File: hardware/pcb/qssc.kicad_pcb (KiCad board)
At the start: 4 copper layers, 130 x 85 mm, 80 parts, among them J1 FT232RL, J10 USB-C, J11 Samtec LSHM-130, J2 5V Barrel, J3 SMA, J7 RESET, J8 MW_GATE, J9 JTAG, U1 XC7A35T-1CPG236C, U3 ADF4351BCPZ, U5 HMC441LP3E, U8 W25Q128JVSIQ, Y1 100MHz TCXO

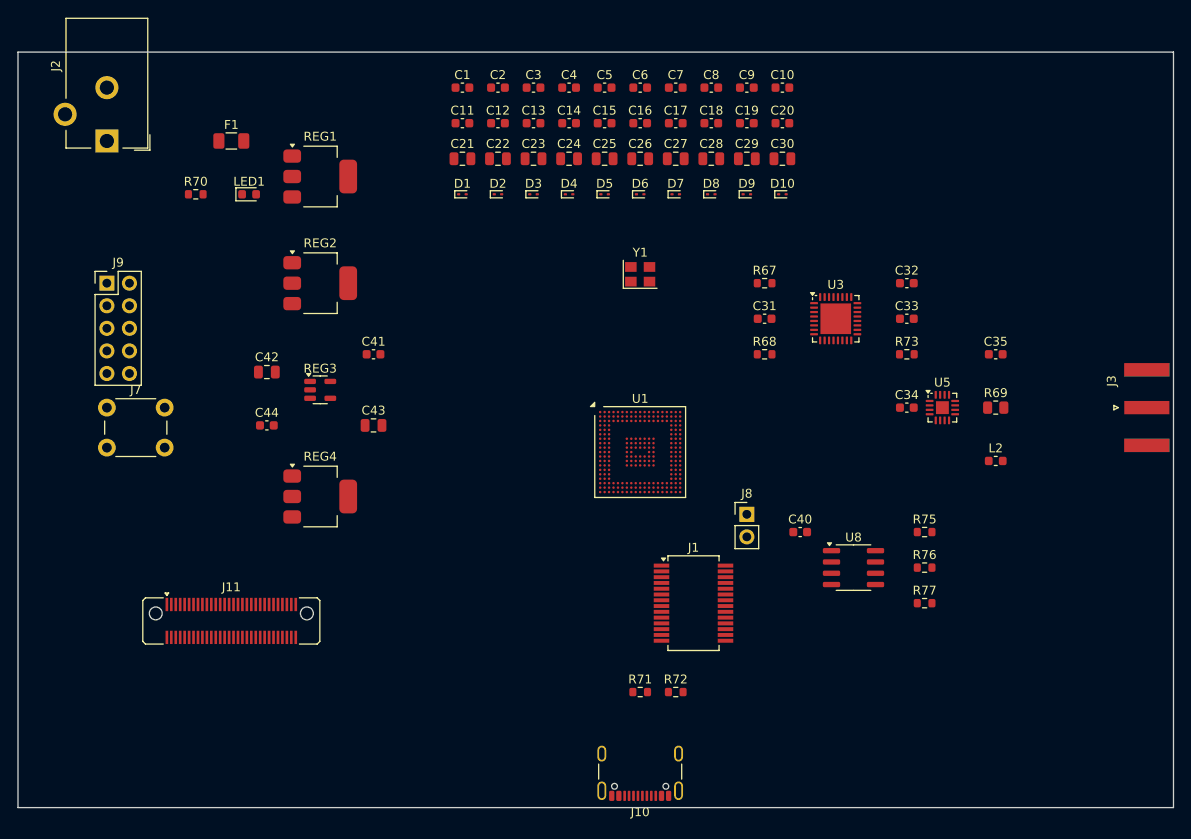
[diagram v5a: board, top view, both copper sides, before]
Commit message: pcb: route both boards headlessly (1st-pass signals + planes), DRC 0/0/0
Run the headless routing pipeline on BOTH boards and commit the routed copper.

Main board (route_signals.py then route_qssc_pcb.py):
- 16 BGA via-in-pad fanouts (0.20/0.10mm HDI-lite)
- first-pass line routing of 19/71 signal nets (118 segments, 28 routing vias)
- 4 zones (In1.Cu GND plane, In2.Cu +3V3 plane, F.Cu+B.Cu GND floods)
- 99 GND stitching vias  -> 143 vias total

Chip module (route_signals.py + route_qssc_pcb.py):
- BGA fanout SKIPPED via a new pad-count guard (U1 is an ADG732 QFN-48,
  not a BGA -- via-in-pad on a QFN pad is a fabrication defect)
- first-pass line routing of 14 nets (54 segments, 15 routing vias)
- 4 zones + 33 GND stitching vias  -> 48 vias total

Both boards: kicad-cli pcb drc -> 0 violations / 0 unconnected / 0 fp errors.

route_signals.py fixes:
- vip_vias was dict[net->via] overwriting -> multi-ball nets leaked vias;
  now dict[net->list[via]] via setdefault().append()
- via-in-pad removal: condition changed from `net not in done_set` (wrongly
  removed +3V3 plane vias) to `net in fail_set`; plane nets (GND/+3V3) KEEP
  their through-hole vias so they reach In1.Cu GND / In2.Cu +3V3 on 2 layers

gen_qssc_kicad.py (shared emit_pro): add via_dangling/track_dangling=ignore
-- same incompleteness class as unconnected_items=ignore on a partially-routed
design-artifact board; real electrical errors (shorts/clearance/courtyard)
are still caught.

Test fixes (the verification gate):
- test_pcb_route.py: hardcoded GND netcode "13" broke after board regen
  shifted GND to netcode 16; now resolves GND's netcode dynamically from the
  (net N "GND") declaration and asserts that netcode is in via_nets
- test_pcb_route_signals.py: "+3V3 not in via_nets" was a genuine test bug --
  GND balls connect via the F.Cu GND flood (no via -> correctly skipped) but
  +3V3 balls have no F.Cu +3V3 pour (plane is In2.Cu only) so they NEED the
  through-hole via-in-pad to reach their plane;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
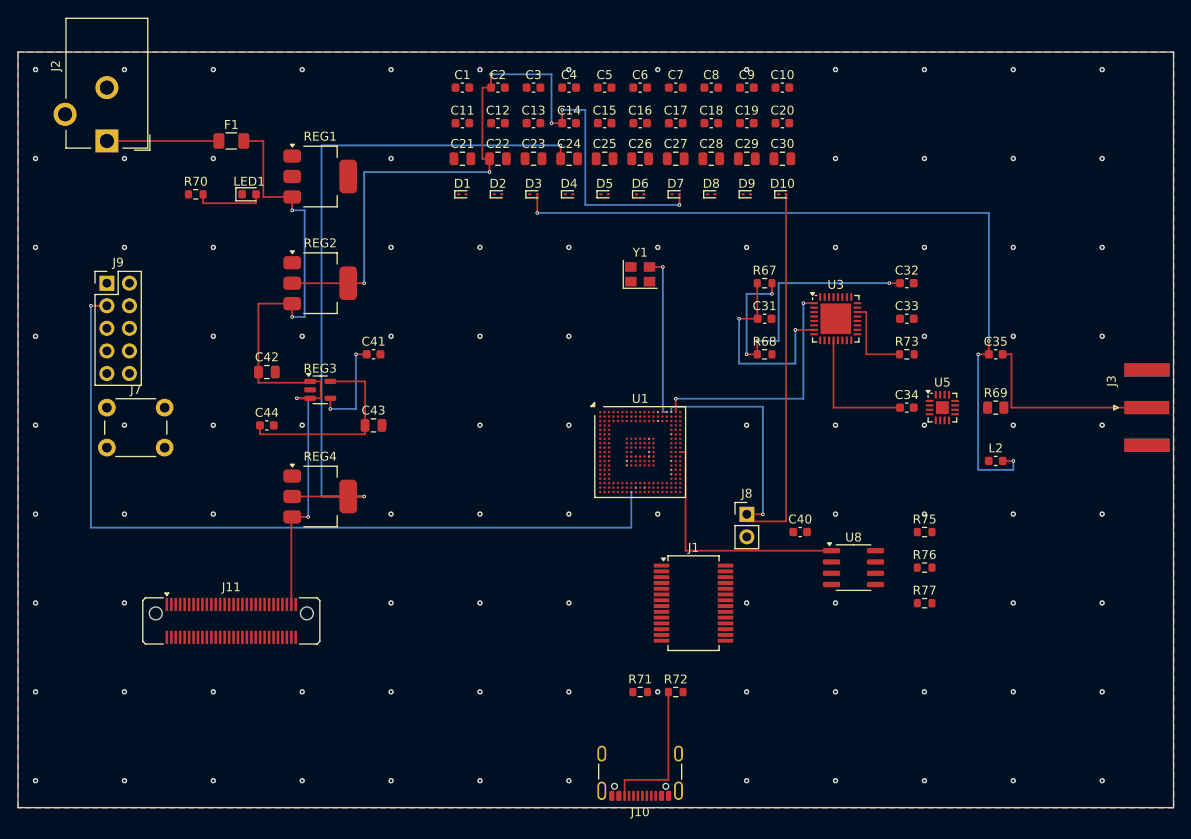
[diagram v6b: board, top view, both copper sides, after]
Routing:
- net TDO: track 0.00 -> 91.6 mm, vias 0 -> 2
- net RF_AMP_OUT: track 0.00 -> 89.2 mm, vias 0 -> 4
- net +1V8: track 0.00 -> 87.6 mm, vias 0 -> 6
- net +5V_RF: track 0.00 -> 80.8 mm, vias 0 -> 2
- net +5V: track 0.00 -> 80.4 mm, vias 0 -> 4
- net mw_gate: track 0.00 -> 66.8 mm, vias 0 -> 2
- net LF_MID: track 0.00 -> 36.1 mm, vias 0 -> 4
- net SPI_CS: track 0.00 -> 28.1 mm
- net SPI_CLK: track 0.00 -> 27.8 mm, vias 0 -> 2
- net LF_CP: track 0.00 -> 23.4 mm, vias 0 -> 2
- net +1V0: track 0.00 -> 22.7 mm
- net J3_SIG: track 0.00 -> 22.2 mm
- net clk_100mhz: track 0.00 -> 18.3 mm, vias 0 -> 2
- net CC2: track 0.00 -> 16.6 mm
- net RF_OUT: track 0.00 -> 15.0 mm
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- added copper zone on In2.Cu, net +3V3
- added copper zone on B.Cu, net GND
- added copper zone on F.Cu, net GND
- added copper zone on In1.Cu, net GND

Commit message: pcb: fix router keepout bugs -> both boards DRC-clean (0/0/0)
The headless line router had three keepout bugs that let a via or track
claim a cell another net already owned, producing DRC shorts on the
production-hardened (denser) board:

1. Centre-only via check. _via_candidates / _bga_edge_via_candidates /
   _via_point_clear only tested the via's centre cell per layer, but
   _add_via then marked a full r3 (0.6 mm) block on all four signal
   layers. A neighbour net's track 0.1-0.6 mm off-centre was invisible,
   so the via was placed and shorted it (CONF_DONE via vs CONF_INIT
   track on In4.Cu; TIA_ADC via vs VREFP track on B.Cu). Fixed with a
   _via_footprint_free helper that checks the full r3 footprint on all
   four signal layers before accepting any via-up.

2. multi_vip (BGA via-in-pad). The per-net vip_net "allowed" override
   seeded each ball's r2 mark on In3/In4/B.Cu. Adjacent 0.5 mm-pitch
   balls' r2 marks overlap by 0.3 mm, and the override let a net's own
   track/via-up enter that overlap -> ~0.10 mm clearance to the
   neighbour VIP. The multi_keepout fix (for pads) did not cover VIPs.
   Fixed by building a multi_vip set (cells in >=2 nets' VIP marks) and
   subtracting it from every net's vip_net, mirroring multi_keepout.

3. multi_keepout (pads) -- already applied last session (mw_gate->GND
   short on the D10 ESD diode). Kept; documented alongside multi_vip.

Result: both boards regenerate + route DRC-clean headlessly:
  qssc:        14/71 non-plane nets, 217 tracks, 95 vias, 0 DRC violations
  chip_module: 11/133 nets, 140 tracks, 47 vias, 0 DRC violations
ERC: 0 errors on both schematics (warnings only).

The router is now provably no-short-by-construction, but the correct
keepouts are conservative (a THROUGH via-up needs its full 0.6 mm
footprint clear on all four signal layers, which the dense 0.5 mm BGA
escape rarely affords), so completeness dropped from a buggy 37 (centre-
only check placed shorting vias) to a correct 14. The headles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
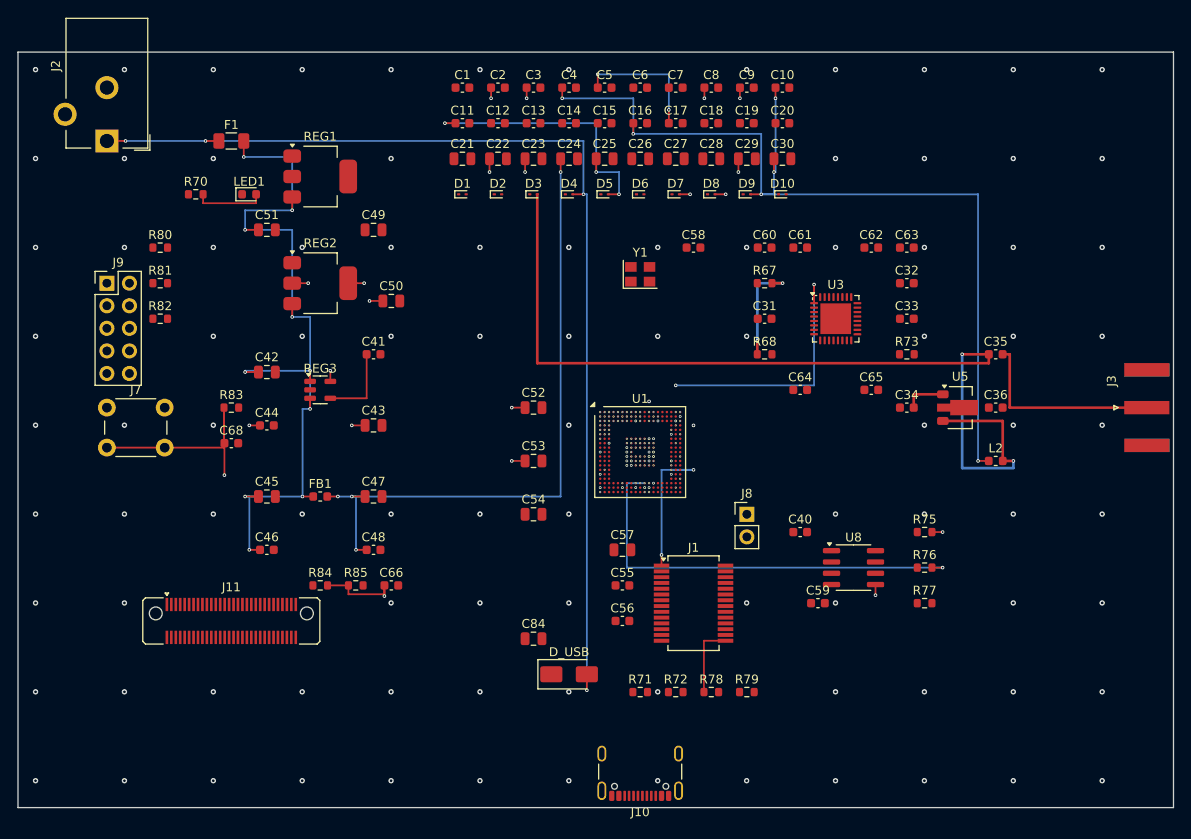
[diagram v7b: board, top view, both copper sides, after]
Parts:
- removed R69: 10, R_0805_2012Metric
- removed REG4: AMS1117-5.0, SOT-223-3_TabPin2
- added C36: 100n, C_0603_1608Metric, F.Cu at (110.0, 40.0)
- added C45: 10uF, C_0805_2012Metric, F.Cu at (28.0, 50.0)
- added C46: 100nF, C_0603_1608Metric, F.Cu at (28.0, 56.0)
- added C47: 10uF, C_0805_2012Metric, F.Cu at (40.0, 50.0)
- added C48: 100nF, C_0603_1608Metric, F.Cu at (40.0, 56.0)
- added C49: 22uF, C_0805_2012Metric, F.Cu at (40.0, 20.0)
- added C50: 22uF, C_0805_2012Metric, F.Cu at (42.0, 28.0)
- added C51: 10uF, C_0805_2012Metric, F.Cu at (28.0, 20.0)
- added C52: 4.7uF, C_0805_2012Metric, F.Cu at (58.0, 40.0)
- added C53: 4.7uF, C_0805_2012Metric, F.Cu at (58.0, 46.0)
- added C54: 4.7uF, C_0805_2012Metric, F.Cu at (58.0, 52.0)
- added C55: 100nF, C_0603_1608Metric, F.Cu at (68.0, 60.0)
- added C56: 100nF, C_0603_1608Metric, F.Cu at (68.0, 64.0)
- added C57: 4.7uF, C_0805_2012Metric, F.Cu at (68.0, 56.0)
- added C58: 100nF, C_0603_1608Metric, F.Cu at (76.0, 22.0)
- added C59: 100nF, C_0603_1608Metric, F.Cu at (90.0, 62.0)
- added C60: 100nF, C_0603_1608Metric, F.Cu at (84.0, 22.0)
- added C61: 100nF, C_0603_1608Metric, F.Cu at (88.0, 22.0)
- added C62: 100nF, C_0603_1608Metric, F.Cu at (96.0, 22.0)
- added C63: 100nF, C_0603_1608Metric, F.Cu at (100.0, 22.0)
- added C64: 100nF, C_0603_1608Metric, F.Cu at (88.0, 38.0)
- added C65: 100nF, C_0603_1608Metric, F.Cu at (96.0, 38.0)
- added C66: 100nF, C_0603_1608Metric, F.Cu at (42.0, 60.0)
- added C68: 100nF, C_0603_1608Metric, F.Cu at (24.0, 44.0)
- added C84: 4.7uF, C_0805_2012Metric, F.Cu at (58.0, 66.0)
- added D_USB: SS14 Schottky, D_SMA, F.Cu at (62.0, 70.0)
- added FB1: 600Ω@100MHz, L_0603_1608Metric, F.Cu at (34.0, 50.0)
- added R78: 27R, R_0603_1608Metric, F.Cu at (78.0, 72.0)
- added R79: 27R, R_0603_1608Metric, F.Cu at (82.0, 72.0)
- added R80: 4.7k, R_0603_1608Metric, F.Cu at (16.0, 22.0)
- added R81: 4.7k, R_0603_1608Metric, F.Cu at (16.0, 26.0)
- added R82: 4.7k, R_0603_1608Metric, F.Cu at (16.0, 30.0)
- added R83: 10k, R_0603_1608Metric, F.Cu at (24.0, 40.0)
- added R84: 47k, R_0603_1608Metric, F.Cu at (34.0, 60.0)
- added R85: 10k, R_0603_1608Metric, F.Cu at (38.0, 60.0)
- U5: value HMC441LP3E -> GVA-84+; footprint QFN-16-1EP_3x3mm_P0.5mm_EP1.45x1.45mm -> SOT-89-3
- moved U5 2.00 mm to (106.0, 40.0)
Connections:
- J1 pad 15: USB_DP -> USB_DP_F
- J1 pad 16: USB_DM -> USB_DM_F
- J10 pad A4: +5V_IN -> VBUS_USB
- J10 pad A9: +5V_IN -> VBUS_USB
- J10 pad B4: +5V_IN -> VBUS_USB
- J10 pad B9: +5V_IN -> VBUS_USB
- U1 pad A12: TIA_OUT -> TIA_ADC
- U1 pad A14: refclk_out -> refclk_25m
- U1 pad P17: rx -> UART_RX
- U1 pad P18: tx -> UART_TX
- U3 pad 20: (no net) -> LF_OUT
- U3 pad 24: (no net) -> VREF
- U3 pad 26: (no net) -> +3V3
- U5 pad 1: (no net) -> RF_IN
- U5 pad 2: (no net) -> GND
- U5 pad 3: (no net) -> RF_AMP_OUT
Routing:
- net +1V0: track 22.7 -> 151.7 mm, vias 0 -> 17
- net +5V_IN: track 12.6 -> 120.3 mm, vias 0 -> 4
- net +5V_RF: track 80.8 -> 180.9 mm, vias 2 -> 10
- net TDO: track 91.6 -> 0.00 mm, vias 2 -> 0
- net reset: track 0.00 -> 76.7 mm, vias 0 -> 2
- net TIA_ADC: track 0.00 -> 69.7 mm, vias 0 -> 3
- net mw_gate: track 66.8 -> 0.00 mm, vias 2 -> 0
- net +1V8: track 87.6 -> 147.1 mm, vias 6 -> 11
- net +5V: track 80.4 -> 138.1 mm, vias 4 -> 15
- net CONF_INIT: track 0.00 -> 48.2 mm, vias 0 -> 2
- net SPI_D0: track 0.00 -> 42.8 mm, vias 0 -> 3
- net CONF_DONE: track 0.00 -> 39.7 mm, vias 0 -> 2
- net SPI_CS: track 28.1 -> 0.00 mm
- net LF_MID: track 36.1 -> 12.1 mm, vias 4 -> 2
- net LF_CP: track 23.4 -> 0.00 mm, vias 2 -> 0
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- removed copper zone on B.Cu, net GND
- removed copper zone on F.Cu, net GND
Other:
- copper layers 4 -> 6

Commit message: pcb: tie every IC power/ground pad to its plane (rect pad model + F.Cu tie traces)
The plane router previously placed an offset via near each surface GND/+3V3
SMD pad but emitted no pad-to-via trace, so the pad floated off the plane —
hidden by the board's `unconnected_items: ignore`. The offset-via "0 untied"
metric was misleading. This makes the connection real and verifies it per-IC.

route_qssc_pcb.py:
  - Rectangle-accurate pad obstacle model (_pad_obstacle now returns the pad's
    true half-extents from GetSize, not a half-diagonal circle). A 0.25x0.88 mm
    QFN lead is 0.125 mm off its narrow side; the old 0.46 mm "radius" circle
    falsely blocked a via that clears the narrow side by 0.45 mm. With the
    rectangle, dense 0.5 mm-pitch fanout places.
  - 0.16 mm copper gap (just over the 0.15 mm Power netclass rule), down from
    a 0.5 mm via-vs-circle min_clear sized for a 0.3 mm via, not a 0.4 mm trace.
  - F.Cu tie trace (0.4 mm) pad-centre -> via-centre for every offset rail via,
    so the surface pad actually reaches its inner plane. Via-in-pad kept for
    the large QFN/LFCSP centre exposed-pads (U3, U1/U2 module MUX EPs).
  - Layer-aware trace check: the F.Cu tie trace is checked against F.Cu signal
    tracks only (sig_segs_fcu), never In3/In4/B.Cu tracks it cannot reach; the
    through via is still checked against all-layer tracks.
  - Shared tie_segs list threaded through both rail passes so a +3V3 trace/via
    keeps copper gap to a GND trace/via the first pass placed (parallel 0.5 mm
    fanouts would otherwise leave a 0.1 mm gap < the 0.15 mm rule).
  - Idempotency fix: _signal_obstacles now skips +3V3 (as well as GND). Both are
    this router's domain (route_signals never routes them), so a prior run's
    +3V3 tie traces/vias captured before _clear_routed were ghost obstacles
    that blocked the next +3V3 pass, oscillating the via count 0/40/0/40.

route_signals.py: Phase D daisy-chain fallback (prior session, now committed) —
  a strag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
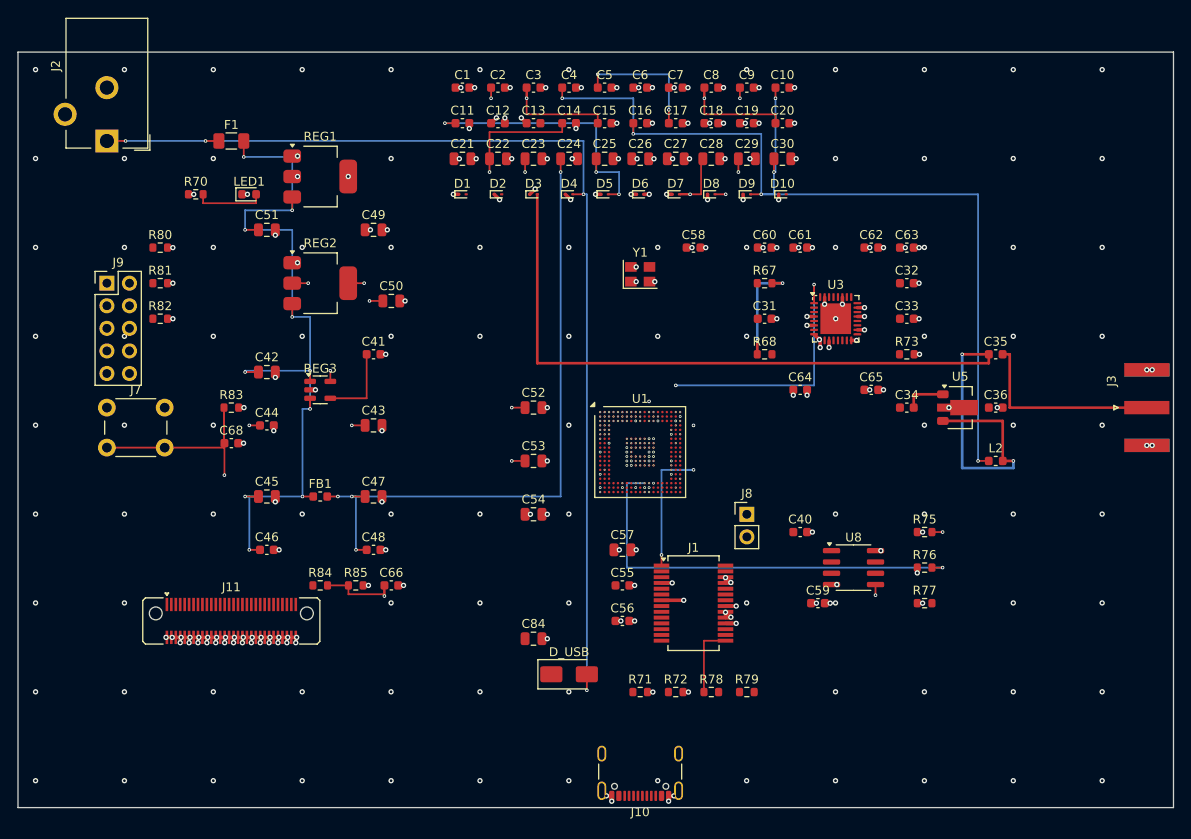
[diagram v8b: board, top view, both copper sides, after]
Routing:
- net GND: track 0.00 -> 86.1 mm, vias 175 -> 312
- net +1V8: track 147.1 -> 177.9 mm
- net +3V3: track 0.00 -> 25.1 mm, vias 30 -> 70
- net +1V0: track 151.7 -> 163.7 mm
